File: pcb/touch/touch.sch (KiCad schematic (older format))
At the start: 20 parts, among them J1 HEADER-1x05, Q1 BSS138, Q2 BSS138, SW1 ALARM, SW2 MENU, SW3 SET, U1 AT42QT1070, U2 LP2981

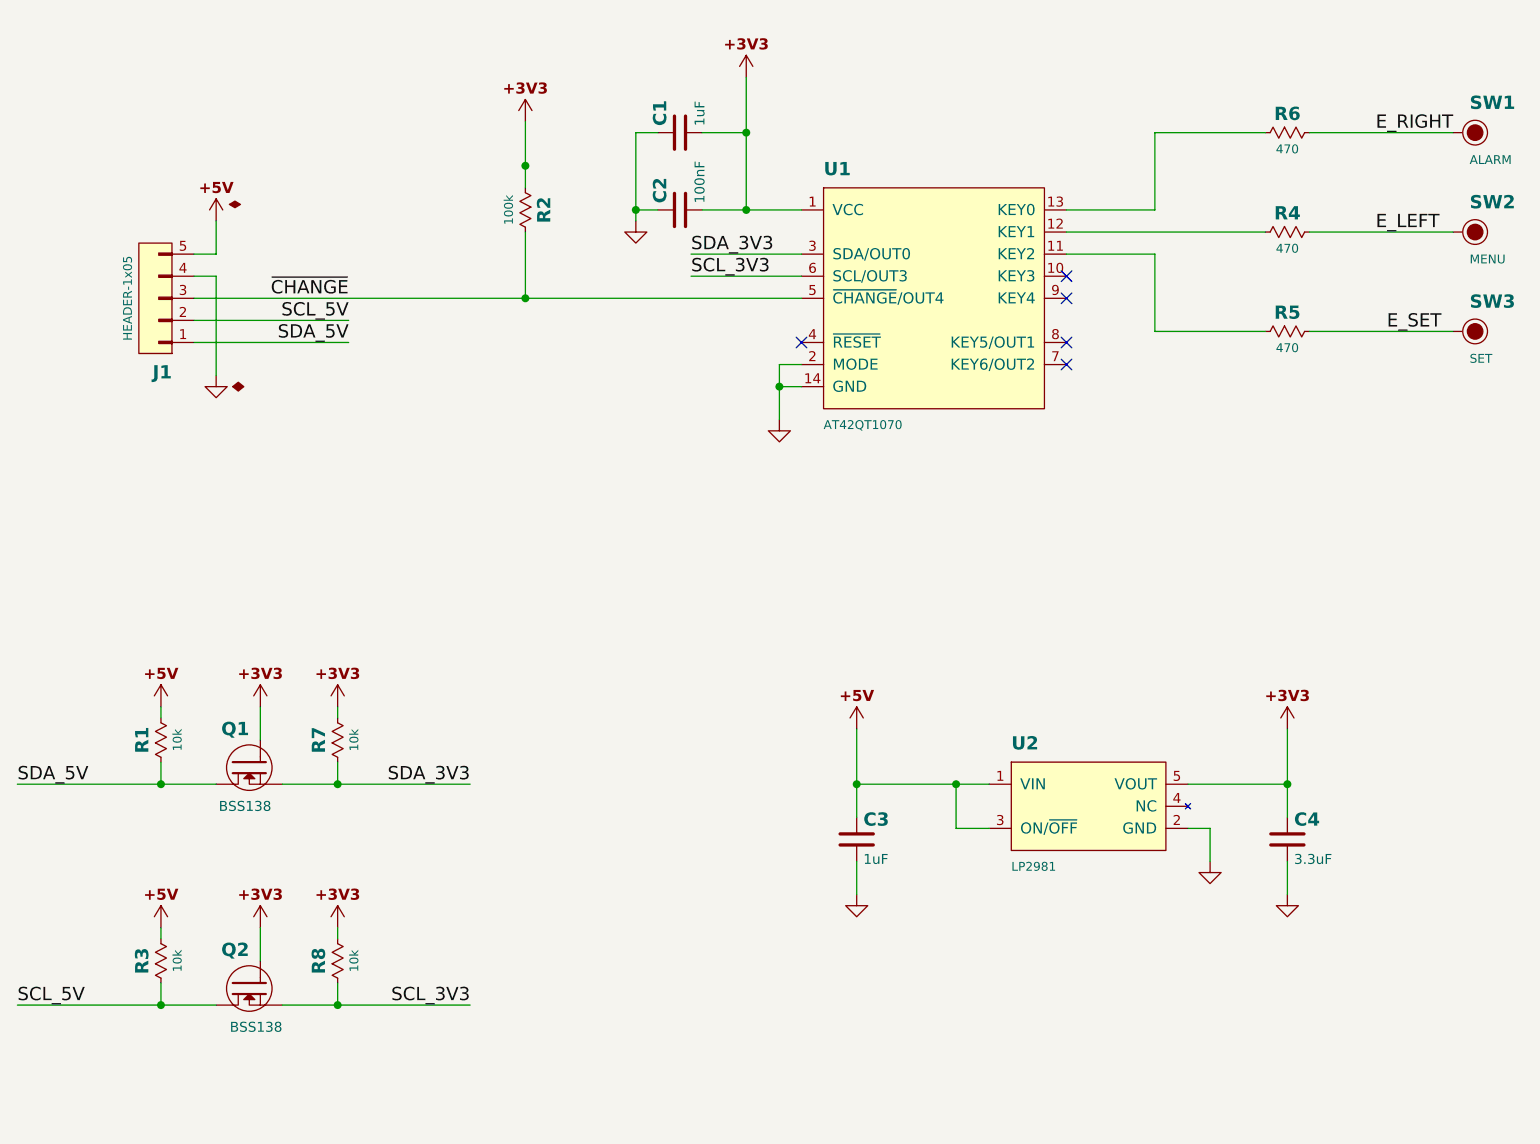
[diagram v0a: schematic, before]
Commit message: * Fix wrong footprint for resistors (C-* to R-*) * Changed schematic sheet size to US letter
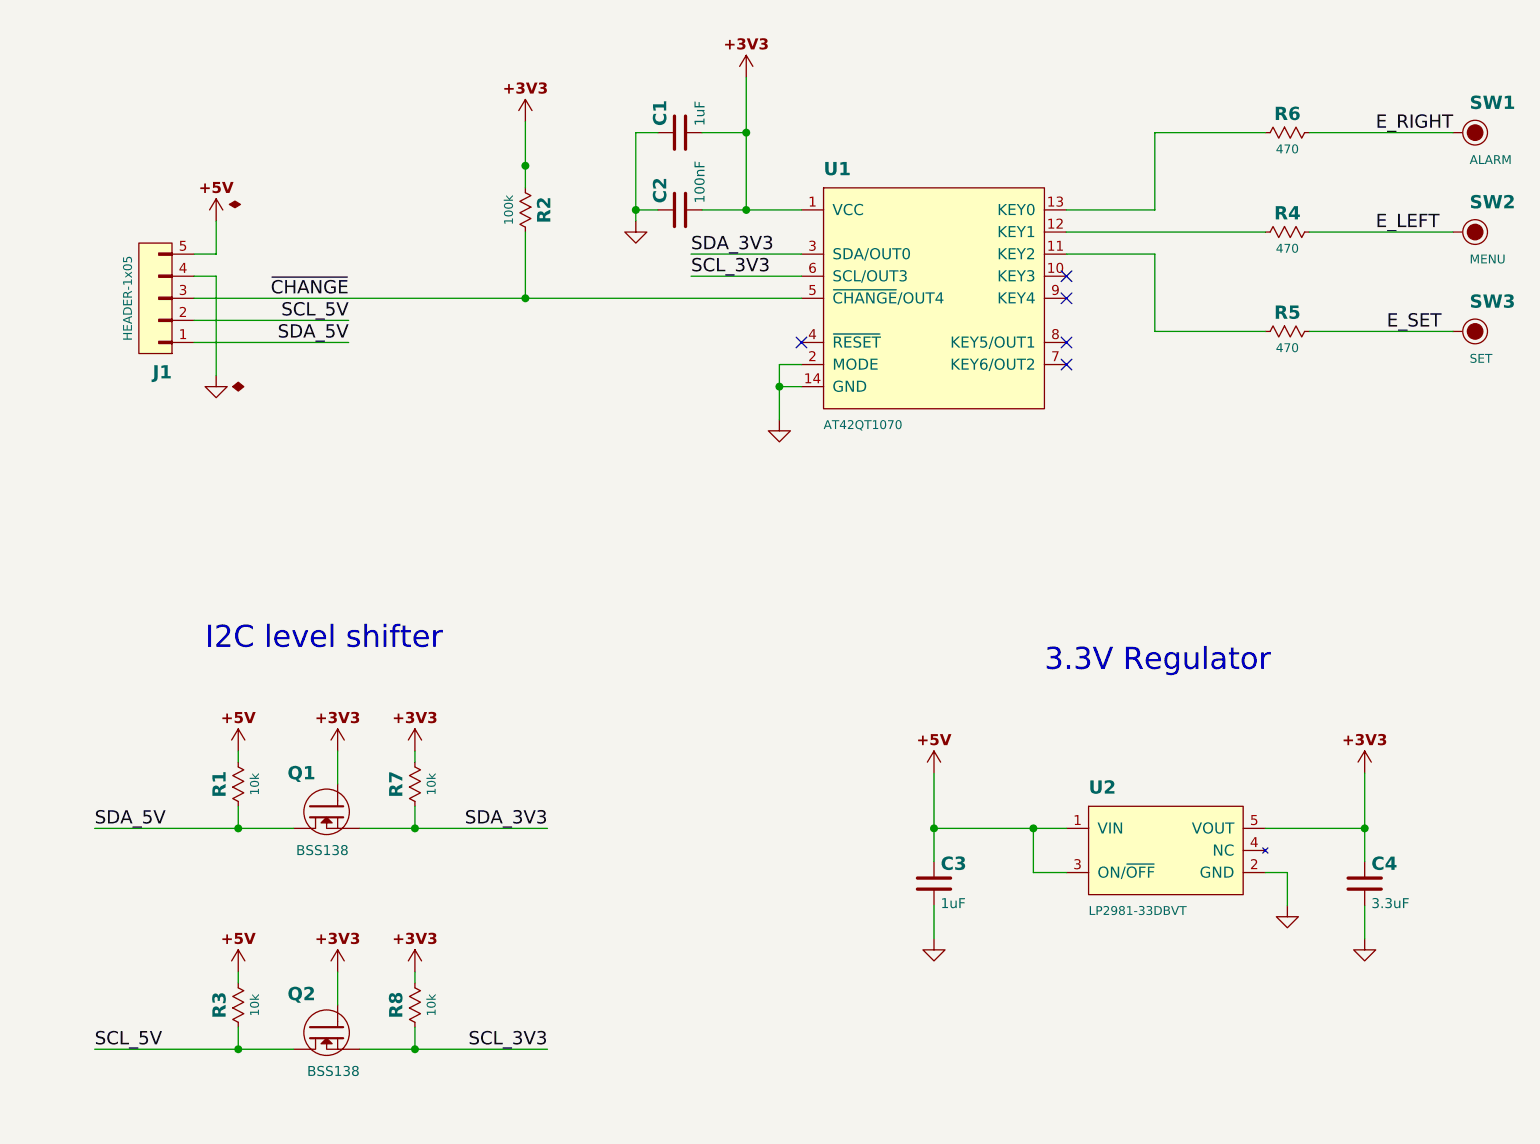
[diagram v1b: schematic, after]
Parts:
- R1, R2, R3, R4, R5, R6, R7, R8: footprint SMT:C-0603 -> SMT:R-0603
- SW1, SW2: footprint Conn-Wire-Pads:touchpad-600x500 -> Conn-Wire-Pads:TouchPad-600x500
- SW3: footprint Conn-Wire-Pads:touchpad-800x500 -> Conn-Wire-Pads:TouchPad-800x500
- U1: footprint SMT-SOIC:14N -> SMT-SOIC:SOIC14N
- U2: value LP2981 -> LP2981-33DBVT
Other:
- note added: "3.3V Regulator"
- note added: "I2C level shifter"
- moved on the sheet: C3, C4, Q1, Q2, R1, R3, R7, R8, U2

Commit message: Revised touch and front panel PCB, Added Motherboard PCB
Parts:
- C1, C3, C4: footprint SMT:C-0805 -> smt:C-0805; symbol CAP -> passive:CAP
- C2: footprint SMT:C-0603 -> smt:C-0603; symbol CAP -> passive:CAP
- J1: footprint Conn-Wire-Pads:WP-50mil-1x05 -> conn-wire-pads:WP-50mil-1x05; symbol HEADER-1x05 -> connectors:HEADER-1x05
- Q1, Q2: footprint SMT-SOT:SOT23 -> smt-sot:SOT23; symbol N-MOSFET -> passive:N-MOSFET
- R1, R2, R3, R4, R5, R6, R7, R8: footprint SMT:R-0603 -> smt:R-0603; symbol RESISTOR -> passive:RESISTOR
- SW1, SW2: footprint Conn-Wire-Pads:TouchPad-600x500 -> conn-wire-pads:TouchPad-700x600; symbol TOUCH-KEY -> touch-rescue:TOUCH-KEY
- SW3: footprint Conn-Wire-Pads:TouchPad-800x500 -> conn-wire-pads:TouchPad-800x600; symbol TOUCH-KEY -> touch-rescue:TOUCH-KEY
- U1: footprint SMT-SOIC:SOIC14N -> smt-soic:SOIC14N; symbol AT42QT1070 -> ic-io:AT42QT1070
- U2: footprint SMT-SOT:SOT23-5 -> smt-sot:SOT23-5; symbol LP2981 -> ic-power:LP2981
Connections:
- net E_LEFT: now also R6.2, SW1.1; no longer R4.2, SW2.1
- net E_RIGHT: now also R4.2, SW2.1; no longer R6.2, SW1.1
- net at U1.10 (KEY3): now also R5.1
- net at U1.11 (KEY2): now also R4.1; no longer R5.1
- net at U1.12 (KEY1): now also R6.1; no longer R4.1
- net at U1.13 (KEY0): no longer R6.1
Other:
- moved on the sheet: C1, C2, C3, C4, J1, Q1, Q2, R1, R2, R3, R4, R5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

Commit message: Updated PCB design
+ Completed daughterboard PCB layout.
* Corrected soldermask clerance on front panel pcb.
- Removed input resistor on DIN for RGB lamp board.
* Modified PCB layout for PSU board.
* Updated gerber files.
* Updated schematics pdf, BOM.
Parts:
- Q1, Q2: symbol passive:N-MOSFET -> transistor:N-MOSFET
- SW1, SW2, SW3: symbol touch-rescue:TOUCH-KEY -> switches:TOUCH-KEY
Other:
- note added: "I2C Addr. : 0x1B"
- moved on the sheet: C1, C2, J1, R2, R4, R5, R6, SW1, SW2, SW3, U1
